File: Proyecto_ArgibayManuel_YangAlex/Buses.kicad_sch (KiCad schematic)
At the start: 6 parts, among them J9 Con_ICSP, U8 MCP2551-I-P, X1 DB9, X2 DB9

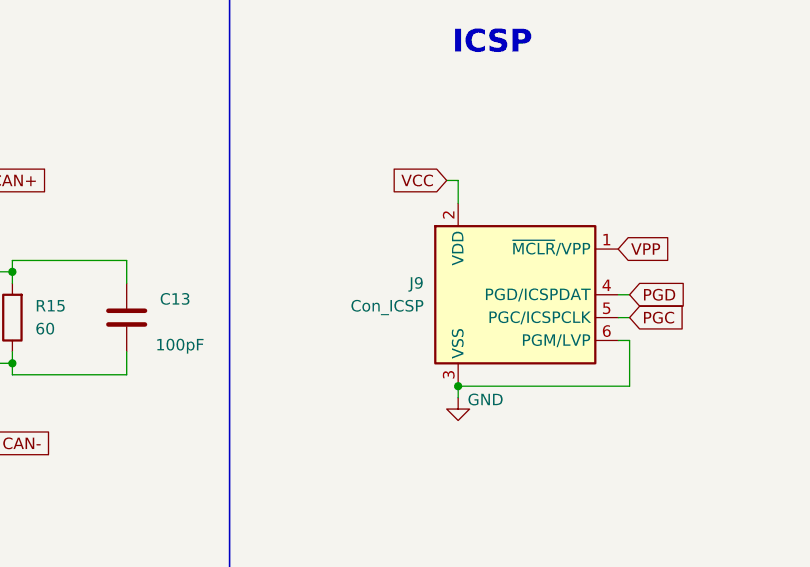
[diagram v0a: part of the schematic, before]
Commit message: cambiar esquematico
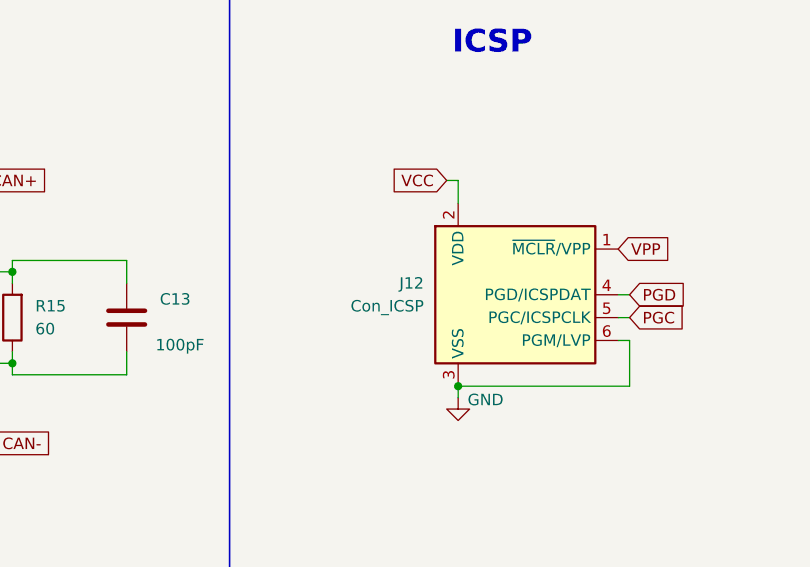
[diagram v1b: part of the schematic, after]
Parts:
- renumbered J9 to J12
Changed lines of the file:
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@@
 		(dnp no)
 		(fields_autoplaced yes)
-		(property "Reference" "#PWR038"
+		(property "Reference" "#PWR041"
 			(at 83.82 100.33 0)
 			(effects
@@
 			(project "Proyecto_ArgibayManuel_YangAlex"
 				(path "/b2dde924-33f5-41ab-a1bf-811873450a89/310eabda-5b3c-4ba2-a48d-a60bed009d94"
-					(reference "#PWR038")
+					(reference "#PWR041")
 					(unit 1)
 				)
@@
 		(dnp no)
 		(fields_autoplaced yes)
-		(property "Reference" "J9"
+		(property "Reference" "J12"
 			(at 209.55 96.5199 0)
 			(effects
@@
 			(project ""
 				(path "/b2dde924-33f5-41ab-a1bf-811873450a89/310eabda-5b3c-4ba2-a48d-a60bed009d94"
-					(reference "J9")
+					(reference "J12")
 					(unit 1)
 				)
@@
 		(on_board yes)
 		(dnp no)
-		(property "Reference" "#PWR041"
+		(property "Reference" "#PWR044"
 			(at 213.36 115.57 0)
 			(effects
@@
 			(project "Proyecto_ArgibayManuel_YangAlex"
 				(path "/b2dde924-33f5-41ab-a1bf-811873450a89/310eabda-5b3c-4ba2-a48d-a60bed009d94"
-					(reference "#PWR041")
+					(reference "#PWR044")
 					(unit 1)
 				)
@@
 		(on_board yes)
 		(dnp no)
-		(property "Reference" "#PWR039"
+		(property "Reference" "#PWR042"
 			(at 132.08 115.57 0)
 			(effects
@@
 			(project "Proyecto_ArgibayManuel_YangAlex"
 				(path "/b2dde924-33f5-41ab-a1bf-811873450a89/310eabda-5b3c-4ba2-a48d-a60bed009d94"
-					(reference "#PWR039")
+					(reference "#PWR042")
 					(unit 1)
 				)
@@
 		(on_board yes)
 		(dnp no)
-		(property "Reference" "#PWR040"
+		(property "Reference" "#PWR043"
 			(at 146.05 116.84 0)
 			(effects
@@
 			(project "Proyecto_ArgibayManuel_YangAlex"
 				(path "/b2dde924-33f5-41ab-a1bf-811873450a89/310eabda-5b3c-4ba2-a48d-a60bed009d94"
-					(reference "#PWR040")
+					(reference "#PWR043")
 					(unit 1)
 				)
@@
 		(on_board yes)
 		(dnp no)
-		(property "Reference" "#PWR037"
+		(property "Reference" "#PWR040"
 			(at 60.96 116.84 0)
 			(effects
@@
 			(project "Proyecto_ArgibayManuel_YangAlex"
 				(path "/b2dde924-33f5-41ab-a1bf-811873450a89/310eabda-5b3c-4ba2-a48d-a60bed009d94"
-					(reference "#PWR037")
-					(unit 1)
-				)
+					(reference "#PWR040")
+					(unit 1)
+				)

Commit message: layout
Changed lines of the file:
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@@
+	(wire
+		(pts
+			(xy 83.82 93.98) (xy 86.36 93.98)
+		)
+		(stroke
+			(width 0)
+			(type default)
+		)
+	)
 	(wire
 		(pts
@@
 	(symbol
 		(lib_id "power:GND")
-		(at 83.82 93.98 0)
+		(at 86.36 93.98 0)
 		(unit 1)
 		(exclude_from_sim no)
@@
 		(fields_autoplaced yes)
 		(property "Reference" "#PWR041"
-			(at 83.82 100.33 0)
+			(at 86.36 100.33 0)
 			(effects
 				(font
@@
 		)
 		(property "Value" "GND"
-			(at 86.36 95.2499 0)
+			(at 88.9 95.2499 0)
 			(effects
 				(font
@@
 		)
 		(property "Footprint" ""
-			(at 83.82 93.98 0)
+			(at 86.36 93.98 0)
 			(effects
 				(font
@@
 		)
 		(property "Datasheet" ""
-			(at 83.82 93.98 0)
+			(at 86.36 93.98 0)
 			(effects
 				(font
@@
 		)
 		(property "Description" "Power symbol creates a global label with name \"GND\" , ground"
-			(at 83.82 93.98 0)
-			(effects
-				(font
+			(at 86.36 93.98 0)
+			(effects
+				(font

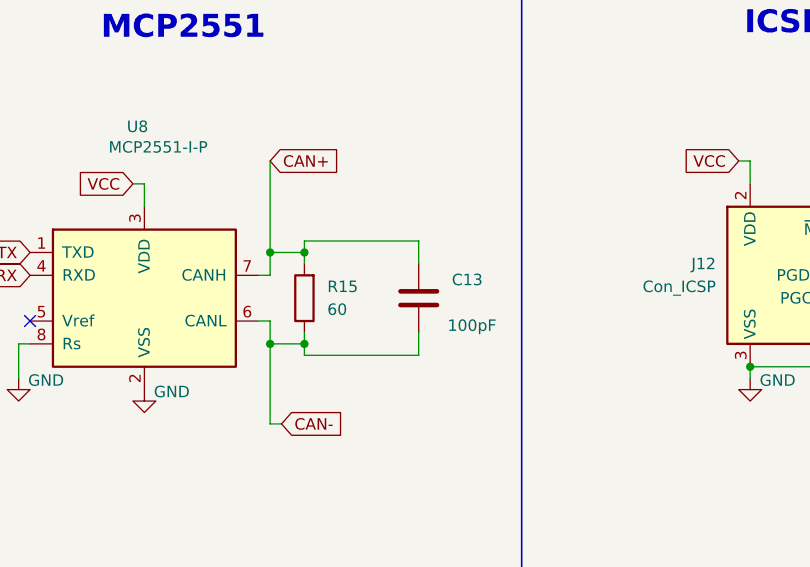
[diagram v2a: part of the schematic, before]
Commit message: Cambio del sensor
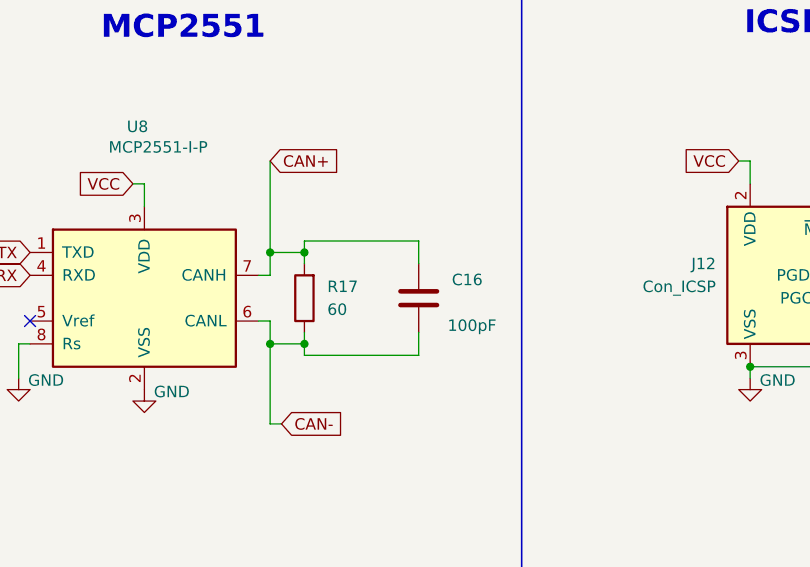
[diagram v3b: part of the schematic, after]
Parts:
- renumbered C13 to C16, R15 to R17
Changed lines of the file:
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@@
 		(dnp no)
 		(fields_autoplaced yes)
-		(property "Reference" "#PWR041"
+		(property "Reference" "#PWR046"
 			(at 86.36 100.33 0)
 			(effects
@@
 			(project "Proyecto_ArgibayManuel_YangAlex"
 				(path "/b2dde924-33f5-41ab-a1bf-811873450a89/310eabda-5b3c-4ba2-a48d-a60bed009d94"
-					(reference "#PWR041")
+					(reference "#PWR046")
 					(unit 1)
 				)
@@
 		(on_board yes)
 		(dnp no)
-		(property "Reference" "#PWR044"
+		(property "Reference" "#PWR049"
 			(at 213.36 115.57 0)
 			(effects
@@
 			(project "Proyecto_ArgibayManuel_YangAlex"
 				(path "/b2dde924-33f5-41ab-a1bf-811873450a89/310eabda-5b3c-4ba2-a48d-a60bed009d94"
-					(reference "#PWR044")
+					(reference "#PWR049")
 					(unit 1)
 				)
@@
 		(on_board yes)
 		(dnp no)
-		(property "Reference" "#PWR042"
+		(property "Reference" "#PWR047"
 			(at 132.08 115.57 0)
 			(effects
@@
 			(project "Proyecto_ArgibayManuel_YangAlex"
 				(path "/b2dde924-33f5-41ab-a1bf-811873450a89/310eabda-5b3c-4ba2-a48d-a60bed009d94"
-					(reference "#PWR042")
+					(reference "#PWR047")
 					(unit 1)
 				)
@@
 		(on_board yes)
 		(dnp no)
-		(property "Reference" "C13"
+		(property "Reference" "C16"
 			(at 183.642 98.298 0)
 			(effects
@@
 			(project "Proyecto_ArgibayManuel_YangAlex"
 				(path "/b2dde924-33f5-41ab-a1bf-811873450a89/310eabda-5b3c-4ba2-a48d-a60bed009d94"
-					(reference "C13")
+					(reference "C16")
 					(unit 1)
 				)
@@
 		(on_board yes)
 		(dnp no)
-		(property "Reference" "R15"
+		(property "Reference" "R17"
 			(at 166.37 99.0599 0)
 			(effects
@@
 			(project "Proyecto_ArgibayManuel_YangAlex"
 				(path "/b2dde924-33f5-41ab-a1bf-811873450a89/310eabda-5b3c-4ba2-a48d-a60bed009d94"
-					(reference "R15")
+					(reference "R17")
 					(unit 1)
 				)
@@
 		(on_board yes)
 		(dnp no)
-		(property "Reference" "#PWR043"
+		(property "Reference" "#PWR048"
 			(at 146.05 116.84 0)
 			(effects
@@
 			(project "Proyecto_ArgibayManuel_YangAlex"
 				(path "/b2dde924-33f5-41ab-a1bf-811873450a89/310eabda-5b3c-4ba2-a48d-a60bed009d94"
-					(reference "#PWR043")
+					(reference "#PWR048")
 					(unit 1)
 				)
@@
 		(on_board yes)
 		(dnp no)
-		(property "Reference" "#PWR040"
+		(property "Reference" "#PWR045"
 			(at 60.96 116.84 0)
 			(effects
@@
 			(project "Proyecto_ArgibayManuel_YangAlex"
 				(path "/b2dde924-33f5-41ab-a1bf-811873450a89/310eabda-5b3c-4ba2-a48d-a60bed009d94"
-					(reference "#PWR040")
-					(unit 1)
-				)
+					(reference "#PWR045")
+					(unit 1)
+				)
